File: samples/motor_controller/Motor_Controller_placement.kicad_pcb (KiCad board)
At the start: 2 copper layers, 64 x 44 mm, 2 parts, among them U1 AP62300, U2 STM32F103C8T6

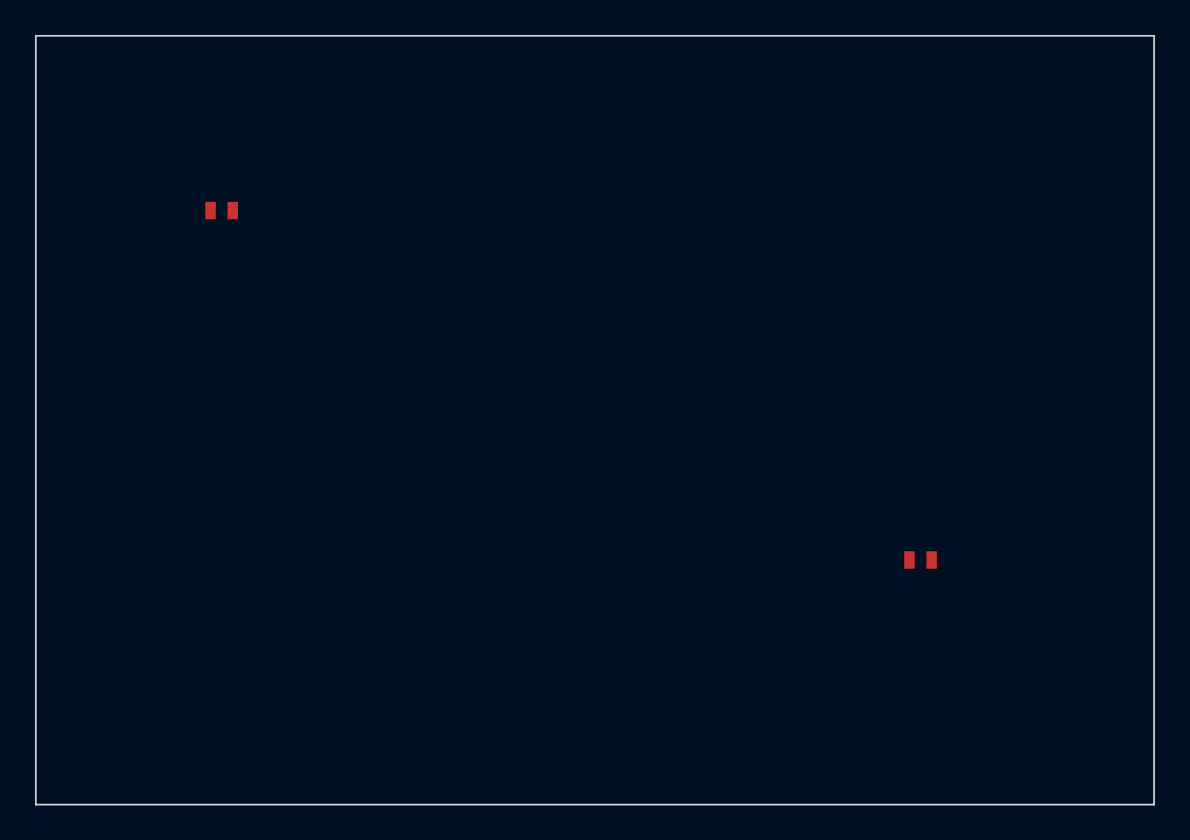
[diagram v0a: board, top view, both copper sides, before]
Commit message: chore: regenerate 8 sample designs against v0.27.0 engine
All 8 samples pass full validation (0 ERC errors):
- led_power_indicator, iot_sensor_node, usb_regulated_supply,
  usb_uart_bridge, oled_display_module, battery_iot_sensor,
  motor_controller, fpga_power_carrier

New artifacts per sample: .kicad_sch, _test_points.csv, _pinout.csv,
canonical_spec.yaml, design_ir.json, validation_report.json; MCU samples
also emit sdkconfig.defaults / .ioc stubs.

Also adds samples/*/svg/ to .gitignore — schematic SVG exports are
regenerable and too large to track.

zigbee_humidistat deferred: non-deterministic schematic output across
two generation runs (text annotation ordering vs sheet_instances).
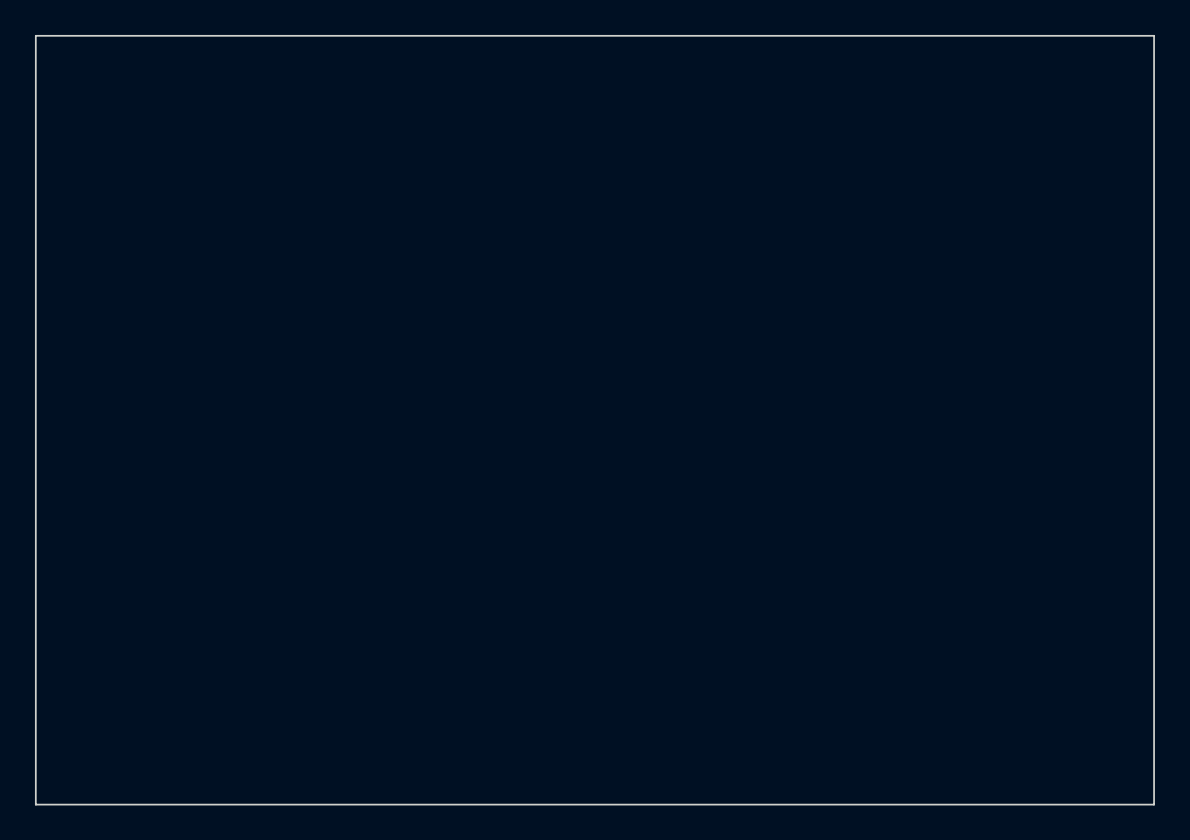
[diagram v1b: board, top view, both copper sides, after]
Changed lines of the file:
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@@
-(kicad_pcb (version 20240108) (generator "schematic_engine")
+(kicad_pcb (version 20240108) (generator "schematic_engine placement_preview")
   (general (thickness 1.6) (legacy_teardrops no))
   (layers
@@
       (effects (font (size 1.0 1.0) (thickness 0.15)))
     )
-    (pad "1" smd rect (at 0.00 0) (size 0.6 1.0) (layers "F.Cu" "F.Paste" "F.Mask") (net 10 "VIN_12V"))
-    (pad "2" smd rect (at 1.27 0) (size 0.6 1.0) (layers "F.Cu" "F.Paste" "F.Mask") (net 4 "GND"))
   )
   (footprint "Package_QFP:LQFP-48_7x7mm_P0.5mm"
@@
       (effects (font (size 1.0 1.0) (thickness 0.15)))
     )
-    (pad "1" smd rect (at 0.00 0) (size 0.6 1.0) (layers "F.Cu" "F.Paste" "F.Mask") (net 9 "VDD_3P3"))
-    (pad "2" smd rect (at 1.27 0) (size 0.6 1.0) (layers "F.Cu" "F.Paste" "F.Mask") (net 4 "GND"))
   )
   (gr_line (start 0.00 0.00) (end 64.00 0.00) (stroke (width 0.1) (type solid)) (layer "Edge.Cuts"))
